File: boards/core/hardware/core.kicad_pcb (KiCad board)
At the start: 2 copper layers, 100 x 100 mm, 87 parts, among them J10 STACK BUS, J11 RACK 12V, J2 ICSP, J20 12V IN, J4 JD0-0004NL, J5 UART, Q1 SUD50P04-08, U1 PIC32MK1024MCM064-I/PT, U2 MCP1826S-3302E/DB, U20 TDN 5-2411WI, U3 W6100-L, Y1 12MHz, Y2 25MHz

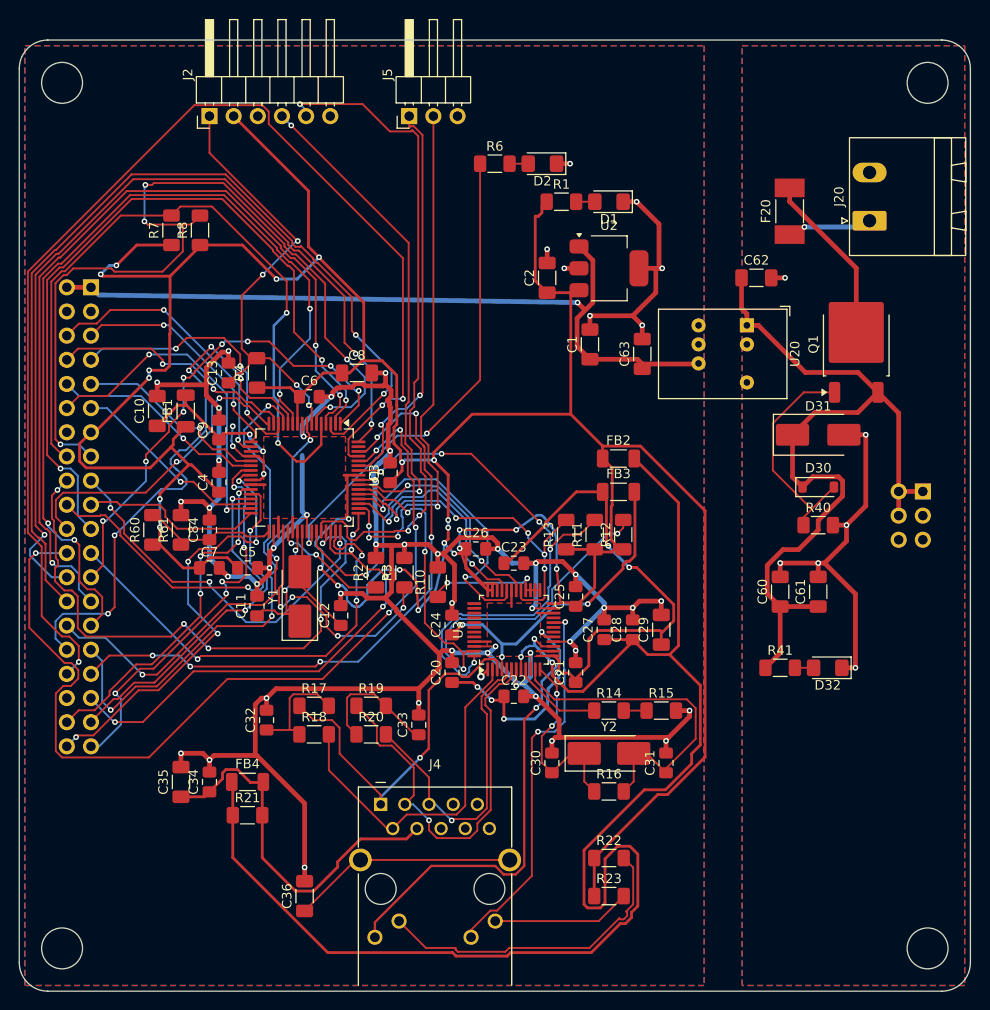
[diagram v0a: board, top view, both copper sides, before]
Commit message: core: finish routing, DRC clean (check_board passes)
- Hand-routed last five connections (user, a88bdbb), then: two +3V3 vias
  0.48 mm apart merged, dangling +5V stub removed, B.Cu GND sliver between
  J10 pins suppressed (GAP_SLIVER_J10 in place.py), mounting holes re-linked
  to Thl_Mechanical (place.py fix), references tidied (silk_tidy.py; U1/U3/Y2
  labelled on the body).
- board.json: core is the top of the stack.
- README: status; open MPNs (25 MHz crystal, 8 pF, 3.3 uF) and stack height.

Co-Authored-By: Claude Opus 5.5 <noreply@anthropic.com>
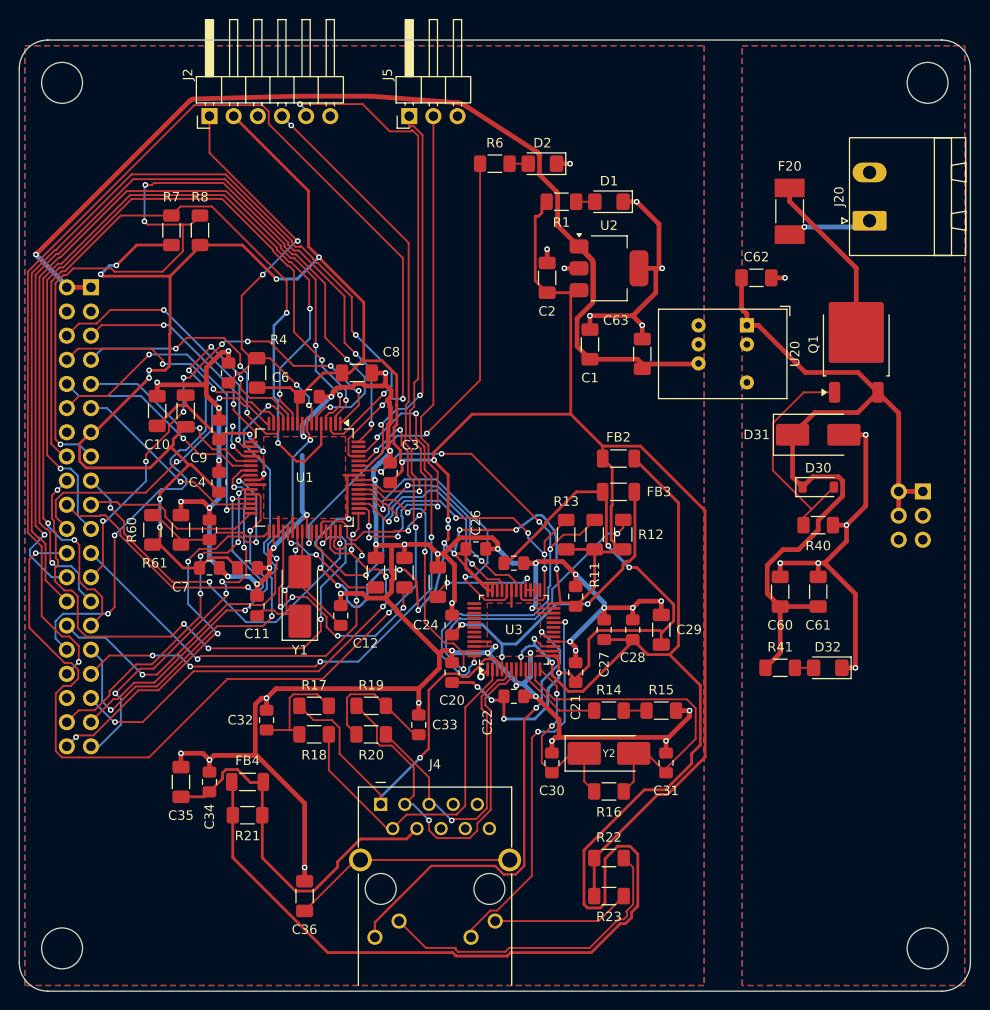
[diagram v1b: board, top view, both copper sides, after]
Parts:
- MH1, MH2, MH3, MH4: footprint MountingHole_4.3mm_M4_Standoff7mm -> Thl_Mechanical:MountingHole_4.3mm_M4_Standoff7mm
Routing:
- net +5V: track 79.5 -> 110.9 mm
- net +3V3: track 388.6 -> 389.0 mm, vias 23 -> 22

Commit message: core: choose Y2/C29/C30/C31, start firmware (CAN card detect + 4 x CAN FD)
Parts: Y2 Abracon ABM3-25.000MHZ-D2Y-T (CL 18 pF) with 27 pF C0G load caps
(same as Y1), C29 Samsung CL31B335KAHVPNE 3.3 uF 25 V X7R. check_board clean.

Firmware (XC32 v5.00, PIC32MK-MC_DFP 1.13.270): 120 MHz via software clock
switch (errata DS80000898D 2.1.1), REFCLK4 40 MHz CAN clock, UART1 console,
W6100 reset/ID/PHY check, can-card detection from the ISOW1044 RXD idle
level, 4 x CAN FD (500k/2M default), loopback self-test.

Co-Authored-By: Claude Opus 5.5 <noreply@anthropic.com>
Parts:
- C30, C31: value 8pF 50V C0G -> 27pF 50V C0G
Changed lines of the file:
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@@
 			)
 		)
-		(property "Manufacturer" "TBD"
+		(property "Manufacturer" "Abracon"
 			(at 0 0 0)
 			(layer "F.Fab")
@@
 			)
 		)
-		(property "MPN" "TBD (25 MHz, 5032, CL 12 pF)"
+		(property "MPN" "ABM3-25.000MHZ-D2Y-T"
 			(at 0 0 0)
 			(layer "F.Fab")
@@
 			)
 		)
-		(property "Manufacturer" "TBD"
+		(property "Manufacturer" "Samsung Electro-Mechanics"
 			(at 0 0 90)
 			(layer "F.Fab")
@@
 			)
 		)
-		(property "MPN" "TBD (3.3 uF 25 V X7R 1206)"
+		(property "MPN" "CL31B335KAHVPNE"
 			(at 0 0 90)
 			(layer "F.Fab")
@@
 			)
 		)
-		(property "Value" "8pF 50V C0G"
+		(property "Value" "27pF 50V C0G"
 			(at 0 1.68 90)
 			(layer "F.Fab")
@@
 			)
 		)
-		(property "Manufacturer" "TBD"
+		(property "Manufacturer" "Murata"
 			(at 0 0 90)
 			(layer "F.Fab")
@@
 			)
 		)
-		(property "MPN" "TBD (8 pF 50 V C0G 0805, to suit the 25 MHz crystal)"
+		(property "MPN" "GRM2165C1H270JA01D"
 			(at 0 0 90)
 			(layer "F.Fab")
@@
 			)
 		)
-		(property "Value" "8pF 50V C0G"
+		(property "Value" "27pF 50V C0G"
 			(at 0 1.68 90)
 			(layer "F.Fab")
@@
 			)
 		)
-		(property "Manufacturer" "TBD"
+		(property "Manufacturer" "Murata"
 			(at 0 0 90)
 			(layer "F.Fab")
@@
 			)
 		)
-		(property "MPN" "TBD (8 pF 50 V C0G 0805, to suit the 25 MHz crystal)"
+		(property "MPN" "GRM2165C1H270JA01D"
 			(at 0 0 90)
 			(layer "F.Fab")

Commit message: Probe test points on all fab boards; golden-board R/C/L test tool
tools/testpoints.py puts a 1.0 mm bare-copper pad (Thl_TestPoint:
TP_Probe_D1.0mm, board-only, no silkscreen) on every net of core,
can-card, io-card, serial-card and can-ssr, only on copper the net
already has (track, via or pour): no routing changes. Clear of foreign
copper, courtyards, all silkscreen, isolation gaps; 0.5 mm from the net's
own pads so the probe measures through the joint. Where nothing fits the
probe point is an SMD pad toe. Bottom-side test points where the parts
are on the bottom (can-ssr). DRC loop moves offenders; check_board clean
on all five boards, no reference texts moved or hidden.

tools/tptest.py: plan (net vs domain ground, across two-pin parts,
isolation between ground domains; powered.csv rail checklist) and run
(golden recording, compare with tolerance + golden spread, serial stream
from the planned probe helper or typed values, current.png step map).
docs/probe-test.md describes the workflow and the helper's interface.

Also: silk_tidy --only and board.json silk_keep; io-card place.py places
the AO row references; place.py scripts ignore TP footprints.

Co-Authored-By: Claude Opus 5.5 <noreply@anthropic.com>
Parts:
- added TP1: pour, Thl_TestPoint:TP_Probe_D1.0mm, F.Cu at (101.6, 108.6)
- added TP10: track, Thl_TestPoint:TP_Probe_D1.0mm, F.Cu at (111.1, 128.4)
- added TP11: track, Thl_TestPoint:TP_Probe_D1.0mm, F.Cu at (128.9, 130.0)
- added TP12: track, Thl_TestPoint:TP_Probe_D1.0mm, F.Cu at (131.2, 129.6)
- added TP13: track, Thl_TestPoint:TP_Probe_D1.0mm, F.Cu at (138.5, 121.1)
- added TP14: track, Thl_TestPoint:TP_Probe_D1.0mm, F.Cu at (140.5, 120.9)
- added TP15: track, Thl_TestPoint:TP_Probe_D1.0mm, F.Cu at (188.0, 124.0)
- added TP16: track, Thl_TestPoint:TP_Probe_D1.0mm, F.Cu at (109.2, 137.4)
- added TP17: track, Thl_TestPoint:TP_Probe_D1.0mm, F.Cu at (109.3, 132.4)
- added TP18: track, Thl_TestPoint:TP_Probe_D1.0mm, F.Cu at (117.6, 131.3)
- added TP19: track, Thl_TestPoint:TP_Probe_D1.0mm, F.Cu at (123.4, 130.3)
- added TP2: pour, Thl_TestPoint:TP_Probe_D1.0mm, F.Cu at (136.1, 101.6)
- added TP20: track, Thl_TestPoint:TP_Probe_D1.0mm, F.Cu at (129.1, 134.3)
- added TP21: track, Thl_TestPoint:TP_Probe_D1.0mm, F.Cu at (134.2, 131.6)
- added TP22: track, Thl_TestPoint:TP_Probe_D1.0mm, F.Cu at (143.5, 137.8)
- added TP23: pour, Thl_TestPoint:TP_Probe_D1.0mm, F.Cu at (145.6, 136.6)
- added TP24: track, Thl_TestPoint:TP_Probe_D1.0mm, F.Cu at (163.6, 133.6)
- added TP25: track, Thl_TestPoint:TP_Probe_D1.0mm, F.Cu at (112.1, 148.9)
- added TP26: track, Thl_TestPoint:TP_Probe_D1.0mm, F.Cu at (113.5, 147.4)
- added TP27: track, Thl_TestPoint:TP_Probe_D1.0mm, F.Cu at (119.3, 142.0)
- added TP28: track, Thl_TestPoint:TP_Probe_D1.0mm, F.Cu at (139.9, 148.7)
- added TP29: track, Thl_TestPoint:TP_Probe_D1.0mm, F.Cu at (147.5, 143.5)
- added TP3: track, Thl_TestPoint:TP_Probe_D1.0mm, F.Cu at (136.7, 107.4)
- added TP30: track, Thl_TestPoint:TP_Probe_D1.0mm, F.Cu at (159.5, 147.5)
- added TP31: track, Thl_TestPoint:TP_Probe_D1.0mm, F.Cu at (169.3, 148.6)
- added TP32: track, Thl_TestPoint:TP_Probe_D1.0mm, F.Cu at (179.2, 145.2)
- added TP33: track, Thl_TestPoint:TP_Probe_D1.0mm, F.Cu at (181.3, 145.1)
- added TP34: track, Thl_TestPoint:TP_Probe_D1.0mm, F.Cu at (106.2, 153.0)
- added TP35: track, Thl_TestPoint:TP_Probe_D1.0mm, F.Cu at (106.5, 150.0)
- added TP36: track, Thl_TestPoint:TP_Probe_D1.0mm, F.Cu at (110.0, 158.3)
- added TP37: track, Thl_TestPoint:TP_Probe_D1.0mm, F.Cu at (110.5, 150.1)
- added TP38: track, Thl_TestPoint:TP_Probe_D1.0mm, F.Cu at (119.1, 159.2)
- added TP39: track, Thl_TestPoint:TP_Probe_D1.0mm, F.Cu at (123.9, 153.8)
- added TP4: pour, Thl_TestPoint:TP_Probe_D1.0mm, F.Cu at (171.6, 101.6)
- added TP40: track, Thl_TestPoint:TP_Probe_D1.0mm, F.Cu at (138.6, 150.6)
- added TP41: track, Thl_TestPoint:TP_Probe_D1.0mm, F.Cu at (140.4, 159.2)
- added TP42: track, Thl_TestPoint:TP_Probe_D1.0mm, F.Cu at (147.3, 157.2)
- added TP43: track, Thl_TestPoint:TP_Probe_D1.0mm, F.Cu at (149.3, 155.4)
- added TP44: track, Thl_TestPoint:TP_Probe_D1.0mm, F.Cu at (151.3, 150.3)
- added TP45: track, Thl_TestPoint:TP_Probe_D1.0mm, F.Cu at (162.8, 156.3)
- added TP46: track, Thl_TestPoint:TP_Probe_D1.0mm, F.Cu at (187.0, 152.7)
- added TP47: track, Thl_TestPoint:TP_Probe_D1.0mm, F.Cu at (111.3, 164.7)
- added TP48: track, Thl_TestPoint:TP_Probe_D1.0mm, F.Cu at (114.9, 162.7)
- added TP49: track, Thl_TestPoint:TP_Probe_D1.0mm, F.Cu at (121.3, 167.7)
- added TP5: track, Thl_TestPoint:TP_Probe_D1.0mm, F.Cu at (121.1, 118.3)
- added TP50: track, Thl_TestPoint:TP_Probe_D1.0mm, F.Cu at (122.2, 161.6)
- added TP51: track, Thl_TestPoint:TP_Probe_D1.0mm, F.Cu at (135.5, 160.1)
- added TP52: track, Thl_TestPoint:TP_Probe_D1.0mm, F.Cu at (113.0, 171.7)
- added TP53: track, Thl_TestPoint:TP_Probe_D1.0mm, F.Cu at (120.5, 175.2)
- added TP54: track, Thl_TestPoint:TP_Probe_D1.0mm, F.Cu at (132.6, 176.8)
- added TP55: track, Thl_TestPoint:TP_Probe_D1.0mm, F.Cu at (136.1, 177.4)
- added TP56: track, Thl_TestPoint:TP_Probe_D1.0mm, F.Cu at (140.0, 171.4)
- added TP57: track, Thl_TestPoint:TP_Probe_D1.0mm, F.Cu at (142.9, 177.4)
- added TP58: track, Thl_TestPoint:TP_Probe_D1.0mm, F.Cu at (153.1, 171.5)
- added TP59: track, Thl_TestPoint:TP_Probe_D1.0mm, F.Cu at (155.7, 172.4)
- added TP6: track, Thl_TestPoint:TP_Probe_D1.0mm, F.Cu at (130.4, 115.9)
- added TP60: track, Thl_TestPoint:TP_Probe_D1.0mm, F.Cu at (169.8, 174.8)
- added TP61: track, Thl_TestPoint:TP_Probe_D1.0mm, F.Cu at (127.8, 188.2)
- added TP62: track, Thl_TestPoint:TP_Probe_D1.0mm, F.Cu at (153.9, 187.9)
- added TP63: track, Thl_TestPoint:TP_Probe_D1.0mm, F.Cu at (153.8, 192.6)
- added TP64: pour, Thl_TestPoint:TP_Probe_D1.0mm, F.Cu at (171.6, 198.6)
- added TP7: track, Thl_TestPoint:TP_Probe_D1.0mm, F.Cu at (148.4, 114.9)
- added TP8: track, Thl_TestPoint:TP_Probe_D1.0mm, F.Cu at (107.1, 124.0)
- added TP9: track, Thl_TestPoint:TP_Probe_D1.0mm, F.Cu at (109.9, 130.0)

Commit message: Mouser cart: SQD50P04-09L P-FET, Diotec P6SMBJ15A TVS
Out of stock: Vishay SUD50P04-08-GE3 (core Q1) -> SQD50P04-09L_GE3 and
Littelfuse SMBJ15A (12 V input TVS) -> Diotec P6SMBJ15A, same footprints,
in core, can-ssr and the can-controller/pic-module references. Logged in
docs/rev-b-changes.md; order lists regenerated. The cart as ordered is
docs/orders/mouser-cart-2026-10-12.xls.

Co-Authored-By: Claude Opus 5.5 <noreply@anthropic.com>
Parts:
- D31: value SMBJ15A -> P6SMBJ15A
- Q1: value SUD50P04-08 -> SQD50P04-09L
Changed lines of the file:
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@@
 			)
 		)
-		(property "Value" "SUD50P04-08"
+		(property "Value" "SQD50P04-09L"
 			(at 0 4.5 90)
 			(layer "F.Fab")
@@
 			)
 		)
-		(property "MPN" "SUD50P04-08-GE3"
+		(property "MPN" "SQD50P04-09L_GE3"
 			(at 0 0 90)
 			(layer "F.Fab")
@@
 			)
 		)
-		(property "Value" "SMBJ15A"
+		(property "Value" "P6SMBJ15A"
 			(at 0 3 0)
 			(layer "F.Fab")
@@
 			)
 		)
-		(property "Manufacturer" "Littelfuse"
+		(property "Manufacturer" "Diotec Semiconductor"
 			(at 0 0 0)
 			(layer "F.Fab")
@@
 			)
 		)
-		(property "MPN" "SMBJ15A"
+		(property "MPN" "P6SMBJ15A"
 			(at 0 0 0)
 			(layer "F.Fab")
